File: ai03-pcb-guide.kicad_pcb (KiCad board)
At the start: 2 copper layers, 93.7 x 38.1 mm, 24 parts, among them SW1 SW_Push, U1 ATmega32U4-AU, Y1 16MHz

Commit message: fill zones
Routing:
- added copper zone on B.Cu, net GND
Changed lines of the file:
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@@
   (segment (start 77.16875 98.425) (end 77.1375 98.45625) (width 0.254) (layer B.Cu) (net 20))
   (segment (start 82.55 98.425) (end 77.16875 98.425) (width 0.254) (layer B.Cu) (net 20))
+  (zone (net 1) (net_name GND) (layer B.Cu) (hatch edge 0.508)
+    (connect_pads (clearance 0.508))
+    (min_thickness 0.254)
+    (fill yes (arc_segments 32) (thermal_gap 0.508) (thermal_bridge_width 0.508))
+    (polygon
+      (pts
+        (xy 46.0375 82.55) (xy 38.1 82.55) (xy 38.1 75.40625) (xy 46.0375 75.40625)
+      )
+    )
+  )
+  (zone (net 1) (net_name GND) (layer B.Cu) (hatch edge 0.508)
+    (connect_pads (clearance 0.508))
+    (min_thickness 0.254)
+    (fill yes (arc_segments 32) (thermal_gap 0.508) (thermal_bridge_width 0.508))
+    (polygon
+      (pts
+        (xy 83.34375 87.3125) (xy 63.5 87.3125) (xy 63.5 78.58125) (xy 83.34375 78.58125)
+      )
+    )
+  )
+  (zone (net 1) (net_name GND) (layer B.Cu) (hatch edge 0.508)
+    (connect_pads (clearance 0.508))
+    (min_thickness 0.254)
+    (fill yes (arc_segments 32) (thermal_gap 0.508) (thermal_bridge_width 0.508))
+    (polygon
+      (pts
+        (xy 76.2 99.21875) (xy 66.675 99.21875) (xy 66.675 89.69375) (xy 76.2 89.69375)
+      )
+    )
+  )
+  (zone (net 1) (net_name GND) (layer B.Cu) (hatch edge 0.508)
+    (connect_pads (clearance 0.508))
+    (min_thickness 0.254)
+    (fill yes (arc_segments 32) (thermal_gap 0.508) (thermal_bridge_width 0.508))
+    (polygon
+      (pts
+        (xy 46.0375 83.34375) (xy 38.1 83.34375) (xy 38.1 75.40625) (xy 46.0375 75.40625)
+      )
+    )
+  )
 )

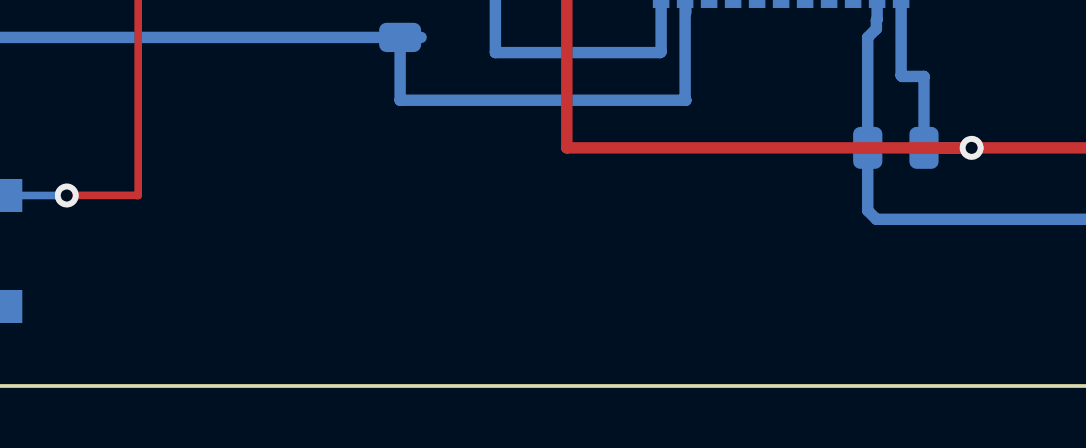
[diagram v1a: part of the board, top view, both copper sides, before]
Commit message: add silkscreen
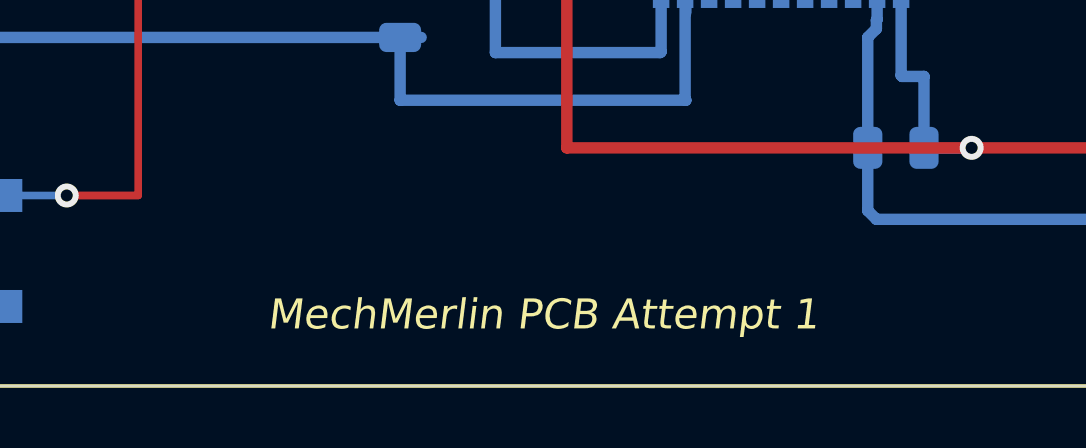
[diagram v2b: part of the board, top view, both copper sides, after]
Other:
- board text added: "MechMerlin PCB Attempt 1"
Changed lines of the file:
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@@
   (general
     (thickness 1.6)
-    (drawings 17)
+    (drawings 18)
     (tracks 209)
     (zones 0)
@@
     )
   )
+  (gr_text "MechMerlin PCB Attempt 1" (at 63.5 111.125) (layer F.SilkS)
+    (effects (font (size 1 1) (thickness 0.15) italic))
+  )
   (gr_line (start 31.75 77.7875) (end 31.75 111.125) (layer Edge.Cuts) (width 0.05))
